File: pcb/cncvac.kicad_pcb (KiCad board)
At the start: 4 copper layers, 48.9 x 59.7 mm, 36 parts, among them J1 AVR-ISP-6, J2 TRIG, SW1 SW_SPST, U1 ATtiny841-SS, U2 MICRF112YMM, U3 LTV-357T, Y1 13.56MHz, Y2 8MHz

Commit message: tweak
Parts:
- added J3: U.FL, Connector_Coaxial:U.FL_Hirose_U.FL-R-SMT-1_Vertical, F.Cu at (77.0, 74.6)
- added R6: 0, Resistor_SMD:R_0402_1005Metric, F.Cu at (76.0, 69.3)
- added R7: 0, Resistor_SMD:R_0402_1005Metric, F.Cu at (76.5, 69.8)
- JP1: moved to B.Cu
- moved JP1 10.6 mm to (38.5, 76.1), turned to -90 degrees
- moved J2 10.2 mm to (38.5, 82.3)
- moved R4 6.17 mm to (40.8, 76.8)
- moved R5 5.94 mm to (40.8, 75.6)
- moved U3 2.02 mm to (46.8, 76.1)
- moved R3 1.75 mm to (50.0, 78.8)
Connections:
- C7 pad 1: Net-(AE1-Pad2) -> Net-(C7-Pad1)
- L2 pad 2: Net-(AE1-Pad2) -> Net-(C7-Pad1)
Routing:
- net /TRIG-: track 5.14 -> 15.8 mm
- net GND: track 27.3 -> 35.8 mm, vias 18 -> 30
- net /TRIG+: track 13.7 -> 9.91 mm, vias 2 -> 1
- net Net-(J3-In): track 0.00 -> 3.73 mm
- net Net-(C7-Pad1): track 0.00 -> 3.56 mm
- net Net-(AE1-Pad2): track 23.4 -> 19.8 mm
- net VDD: track 73.6 -> 70.1 mm
- net Net-(R4-Pad1): track 1.80 -> 4.51 mm
- net /EXT_TRIG: track 13.1 -> 12.0 mm
- net Net-(JP1-A): track 4.04 -> 4.38 mm, vias 0 -> 1
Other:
- board text added: "+"
- board text added: "-"
- board text added: "CASE : 1593PBK (PCB IS NOT SYMMETRICAL)"
- board text added: "Dielectric Constant 4.4 Eff = 3.33"
- board text added: "Hammond 1593P"
- board text added: "Stackup : JLC04161H-7628"
- board text removed: "Stackup : JLC04161H-7628 CASE : 1593PBK (PCB IS NOT SYMMETRICAL)"
- board text removed: "TRIG+"
- board text removed: "TRIG-"

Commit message: add via for rf test
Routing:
- net GND: vias 30 -> 31
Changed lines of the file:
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@@
+	)
+	(via
+		(at 77.424648 68.369377)
+		(size 0.8)
+		(drill 0.5)
+		(layers "F.Cu" "B.Cu")
+		(free yes)
+		(net 18)
 	)
 	(via

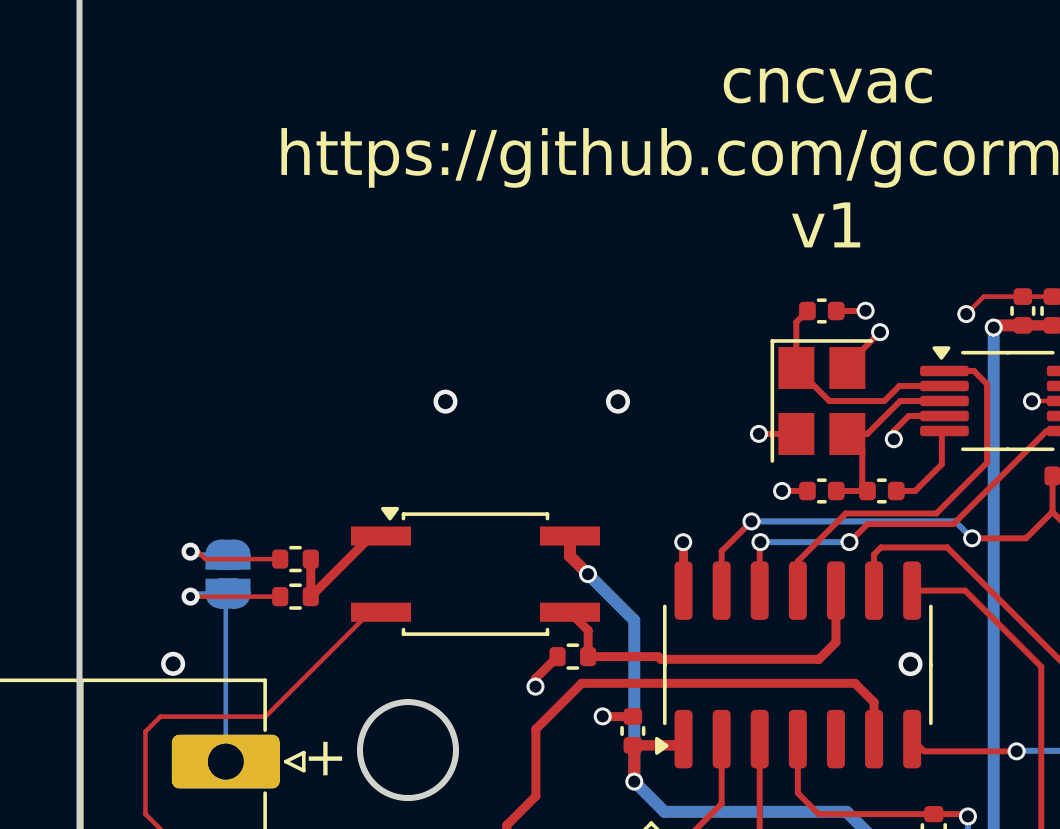
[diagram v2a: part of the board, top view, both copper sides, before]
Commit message: shift the antenna opening in the panel slightly
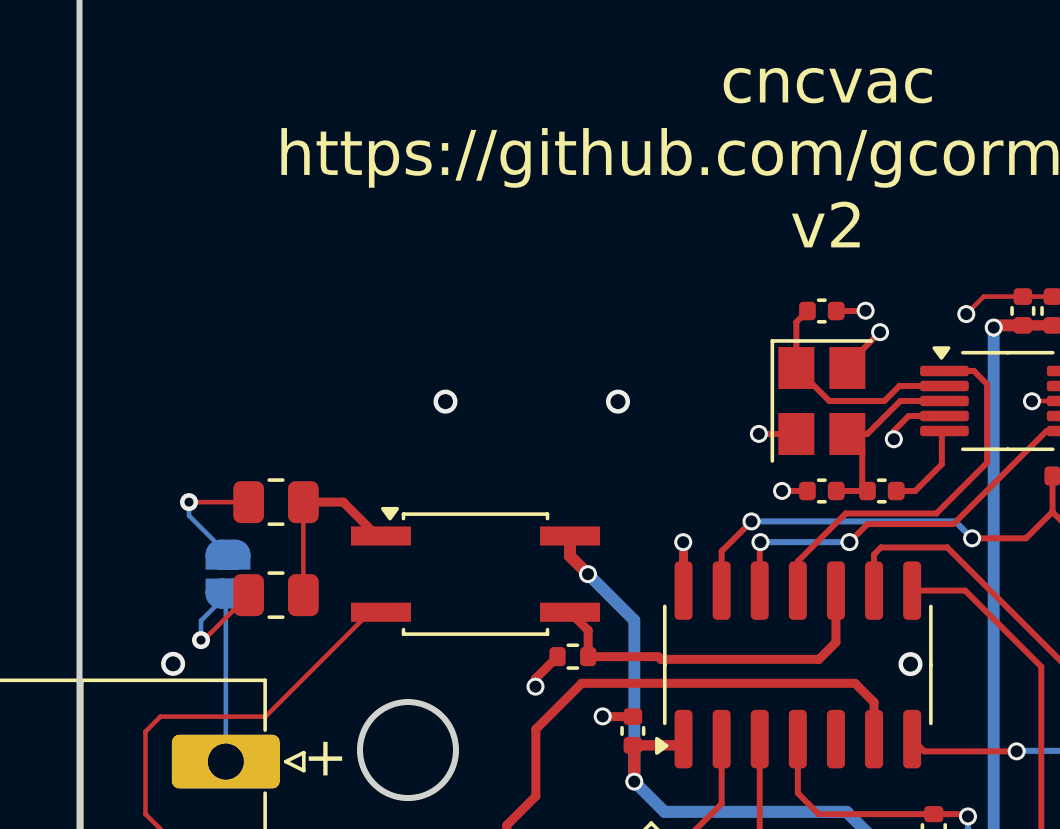
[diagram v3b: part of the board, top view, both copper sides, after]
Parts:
- R4, R5: value 1k -> 22k; footprint Resistor_SMD:R_0402_1005Metric -> Resistor_SMD:R_0805_2012Metric
- moved R5 2.01 mm to (40.1, 73.7)
- moved R4 0.65 mm to (40.1, 76.8)
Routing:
- net Net-(R4-Pad1): track 4.51 -> 6.16 mm
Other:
- board text added: "Solder JP1 bridge to reduce trigger resistor from 22K to 11K"
- board text added: "cncvac https://github.com/gcormier/cncvac v2"
- board text removed: "Solder JP1 bridge to reduce trigger resistor from 1K to 500Ω (Better for 5V input)"
- board text removed: "cncvac https://github.com/gcormier/cncvac v1"

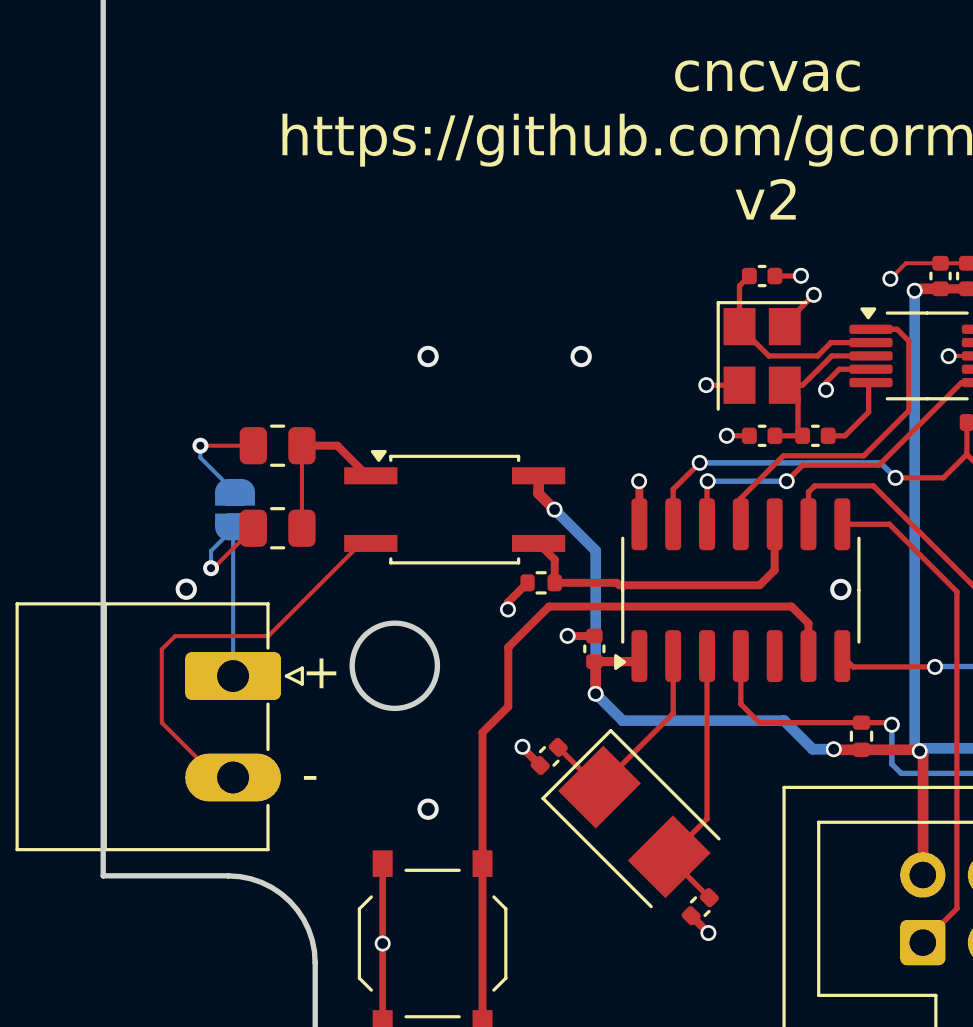
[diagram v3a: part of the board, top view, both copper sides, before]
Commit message: Add protection diode to opto, increase pulldown strength
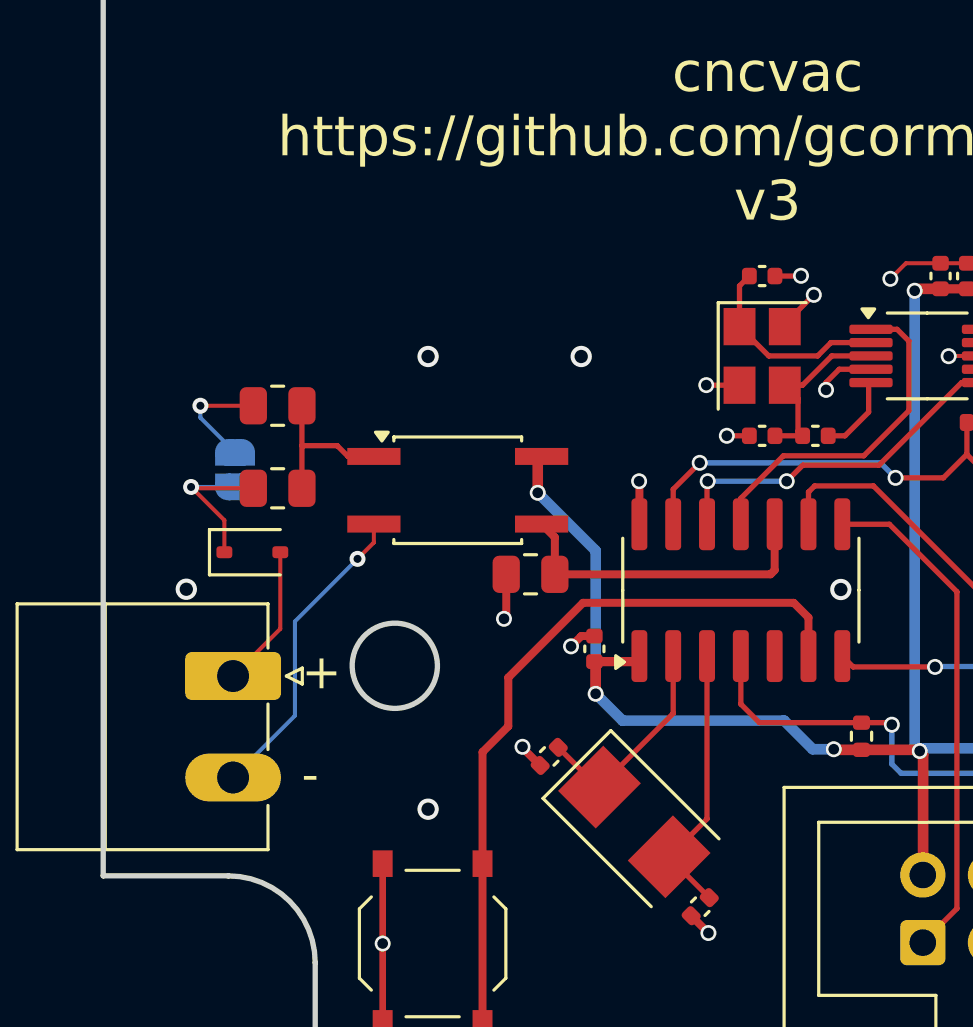
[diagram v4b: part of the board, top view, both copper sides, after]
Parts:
- added D1: 1N5819WS, Diode_SMD:D_SOD-323, F.Cu at (39.2, 77.7)
- R3: value 100k -> 22k; footprint Resistor_SMD:R_0402_1005Metric -> Resistor_SMD:R_0805_2012Metric
- moved JP1 1.50 mm to (38.5, 74.6)
- moved R4 1.50 mm to (40.1, 75.3)
- moved R5 1.50 mm to (40.1, 72.2)
- moved U3 0.74 mm to (46.9, 75.3)
- moved R3 0.51 mm to (49.6, 78.5)
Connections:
- JP1 pad 2: /TRIG+ -> Net-(D1-K)
- R4 pad 2: /TRIG+ -> Net-(D1-K)
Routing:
- net Net-(D1-K): track 0.00 -> 7.08 mm, vias 0 -> 1
- net /TRIG+: track 9.76 -> 5.38 mm, vias 1 -> 0
- net /TRIG-: track 15.8 -> 11.7 mm, vias 0 -> 1
- net VDD: track 70.1 -> 70.9 mm
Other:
- board text added: "cncvac https://github.com/gcormier/cncvac v3"
- board text removed: "cncvac https://github.com/gcormier/cncvac v2"

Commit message: fixup
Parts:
- added JP2: SolderJumper_3_Bridged12, Jumper:SolderJumper-3_P1.3mm_Bridged12_RoundedPad1.0x1.5mm_NumberLabels, B.Cu at (54.0, 69.6)
- added R10: 100k, Resistor_SMD:R_0402_1005Metric, F.Cu at (39.0, 77.6)
- added R11: 100k, Resistor_SMD:R_0402_1005Metric, F.Cu at (46.8, 77.6)
- added R12: 100k, Resistor_SMD:R_0402_1005Metric, F.Cu at (41.5, 77.6)
- added R8: 100k, Resistor_SMD:R_0402_1005Metric, F.Cu at (36.5, 77.6)
- added R9: 100k, Resistor_SMD:R_0402_1005Metric, F.Cu at (44.3, 77.6)
- added SW2: SW_DIP_x05, Button_Switch_THT:SW_DIP_SPSTx05_Slide_9.78x14.88mm_W7.62mm_P2.54mm, F.Cu at (37.1, 75.1)
- SW1: moved to B.Cu
- moved JP1 20.1 mm to (50.0, 91.1), turned to 180 degrees
- moved U3 19.3 mm to (48.0, 94.6)
- moved R3 18.1 mm to (54.8, 95.8), turned to 0 degrees
- moved R5 15.9 mm to (46.3, 86.8), turned to 0 degrees
- moved D1 15.2 mm to (46.3, 91.1), turned to 180 degrees
- moved R4 14.9 mm to (46.3, 88.8), turned to 0 degrees
- moved SW1 9.92 mm to (55.8, 91.1), turned to 90 degrees
- moved J3 5.38 mm to (79.5, 69.8), turned to 0 degrees
- moved BT1 4.49 mm to (77.8, 87.5)
- moved J1 1.48 mm to (64.3, 93.8)
- moved R6 1.01 mm to (75.0, 69.3)
- moved R7 1.01 mm to (75.5, 69.8)
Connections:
- net /MISO renamed /DIP2
- net /MOSI renamed /DIP5
- net /SCK renamed /DIP3
- U1 pad 10: /EXT_TRIG -> /DIP1
- U1 pad 11: /ASK -> /EXT_TRIG
- U1 pad 12: /FSK -> /DATA
- U1 pad 5: unconnected-(U1-PB2-Pad5) -> /DIP4
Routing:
- net /DIP2: track 19.1 -> 49.5 mm, vias 0 -> 1
- net /DIP3: track 23.8 -> 50.5 mm, vias 0 -> 1
- net /DIP1: track 0.00 -> 26.3 mm, vias 0 -> 2
- net /DIP5: track 13.6 -> 39.7 mm
- net /DIP4: track 0.00 -> 23.4 mm
- net /EXT_TRIG: track 12.1 -> 34.7 mm, vias 0 -> 4
- net Net-(SW1-A): track 27.5 -> 13.5 mm, vias 0 -> 1
- net /DATA: track 0.00 -> 7.97 mm, vias 0 -> 1
- net VDD: track 70.9 -> 77.6 mm, vias 5 -> 4
- net /TRIG+: track 5.38 -> 11.9 mm
- net GND: track 36.2 -> 41.9 mm, vias 31 -> 30
- net Net-(D1-K): track 7.08 -> 4.36 mm
- net /FSK: track 13.6 -> 16.3 mm, vias 2 -> 1
- net Net-(R11-Pad1): track 0.00 -> 2.49 mm
- net Net-(R9-Pad1): track 0.00 -> 2.45 mm
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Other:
- outline, holes or cut-outs redrawn
- board text added: "1 2 4 5 6"
- board text added: "Enclosure: Hammond 1593P Bud Industries HP-3661-B"
- board text added: "FSK / ASK Default ASK"
- board text added: "SYS"
- board text added: "Stackup JLC04161H-7628 Material FR4 TG155"
- board text added: "TOOL"
- board text added: "cncvac github.com/gcormier/cncvac v3"
- board text removed: "Hammond 1593P"
- board text removed: "Stackup : JLC04161H-7628"
- board text removed: "cncvac https://github.com/gcormier/cncvac v3"

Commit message: fix silk
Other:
- board text added: "cncvac github.com/gcormier/cncvac <<hash>>"
- board text removed: "<<hash>>"
- board text removed: "cncvac github.com/gcormier/cncvac v3"
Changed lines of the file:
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@@
 		)
 	)
-	(gr_text "cncvac\ngithub.com/gcormier/cncvac\nv3"
-		(at 58.524648 42.069377 0)
+	(gr_text "cncvac\ngithub.com/gcormier/cncvac\n<<hash>>"
+		(at 58.524648 58.389377 0)
 		(layer "F.SilkS")
 		(effects
@@
 		)
 	)
-	(gr_text "<<hash>>"
-		(at 79.944314 47.364377 90)
-		(layer "F.SilkS")
-		(effects
-			(font
-				(size 1 1)
-				(thickness 0.2)
-			)
-			(justify right)
-		)
-	)

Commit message: fix pn for opto
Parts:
- U3: value LTV-357T -> EL357N
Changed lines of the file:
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@@
 		(sheetname "/")
 		(sheetfile "cncvac.kicad_sch")
-		(attr through_hole)
+		(attr through_hole exclude_from_bom dnp)
 		(fp_line
 			(start -21 16.5)
@@
 			)
 		)
-		(property "Value" "LTV-357T"
+		(property "Value" "EL357N"
 			(at 0 2.8 0)
 			(layer "F.Fab")
@@
 			)
 		)
-		(property "LCSC" "C6649"
+		(property "LCSC" "C42381015"
 			(at 0 0 0)
 			(unlocked yes)
